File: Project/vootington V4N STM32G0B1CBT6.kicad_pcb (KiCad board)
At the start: 2 copper layers, 242.9 x 95.2 mm, 334 parts, among them J1 Conn_01x04, J2 USB_C sink board 1.3mm, J3 JST SH, J4 Pico EZmate, Q1 AP40P05, SW1 Alps SKRK, SW2 Alps SKRK, U1 SLSS49E-3, U10 SLSS49E-3, U11 SLSS49E-3, U12 SLSS49E-3, U13 SLSS49E-3, U14 SLSS49E-3, U15 SLSS49E-3, U16 SLSS49E-3, U17 SLSS49E-3, U18 SLSS49E-3, U19 SLSS49E-3, U2 SLSS49E-3, U20 SLSS49E-3, U21 SLSS49E-3, U22 SLSS49E-3, U23 SLSS49E-3, U24 SLSS49E-3, U25 SLSS49E-3, U26 SLSS49E-3, U27 SLSS49E-3, U28 SLSS49E-3, U29 SLSS49E-3, U3 SLSS49E-3, U30 SLSS49E-3, U31 SLSS49E-3, U32 SLSS49E-3, U33 SLSS49E-3, U34 SLSS49E-3, U35 SLSS49E-3, U36 SLSS49E-3, U37 SLSS49E-3, U38 SLSS49E-3, U39 SLSS49E-3, U4 SLSS49E-3, U40 SLSS49E-3, U41 SLSS49E-3, U42 SLSS49E-3, U43 SLSS49E-3, U44 SLSS49E-3, U45 SLSS49E-3, U46 SLSS49E-3, U47 SLSS49E-3, U48 SLSS49E-3, U49 SLSS49E-3, U5 SLSS49E-3, U50 SLSS49E-3, U51 SLSS49E-3, U52 SLSS49E-3, U53 STM32G0B1CBTx, U54 AP2112K-3.3, U55 PRTR5V0U2X, U56 74AHCT1G125, U57 74HC4051, U58 74HC4051, U59 74HC4051, U6 SLSS49E-3, U60 74HC4051, U61 74HC4051, U62 74HC4051, U63 74HC4051, U7 SLSS49E-3, U8 SLSS49E-3, U9 SLSS49E-3

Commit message: revision proto ready
folder clean up
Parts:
- moved G*** 82.7 mm to (132.3, 58.6)
- moved G*** 32.5 mm to (265.1, 46.8), turned to -90 degrees
- moved H9 10.3 mm to (184.2, 60.3)
- moved H16 4.83 mm to (266.7, 69.8)
- moved H14 3.59 mm to (223.8, 69.8)
- moved H13 0.79 mm to (240.5, 41.3)
- moved H1 0.79 mm to (36.5, 22.2)
- moved H6 0.38 mm to (106.7, 69.8)
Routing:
- net GND: track 318.6 -> 333.2 mm, vias 189 -> 195
- net K_36: track 30.3 -> 24.1 mm
- net K_12: track 52.9 -> 49.0 mm
- net ADC0: track 213.2 -> 216.7 mm
- net K_24: track 27.8 -> 25.0 mm
- net K_46: track 42.4 -> 39.9 mm
- net RGB MCU: track 34.8 -> 33.6 mm
- net Net-(D32-DIN): track 18.0 -> 16.8 mm
- net K_26: track 23.9 -> 22.9 mm
- net +5V: track 1292.0 -> 1291.1 mm
- net +3V3: track 259.3 -> 258.4 mm
- net K_31: track 17.9 -> 17.1 mm
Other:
- board text added: "JLCJLCJLCJLC"
- board text removed: "K47!???!!!"
- board text removed: "rearrange layout. add caps reroute and make sure multiplexers have right amount are correct rearrange mounting holes, traymount?? POWER SHIFTER, PINOUT"

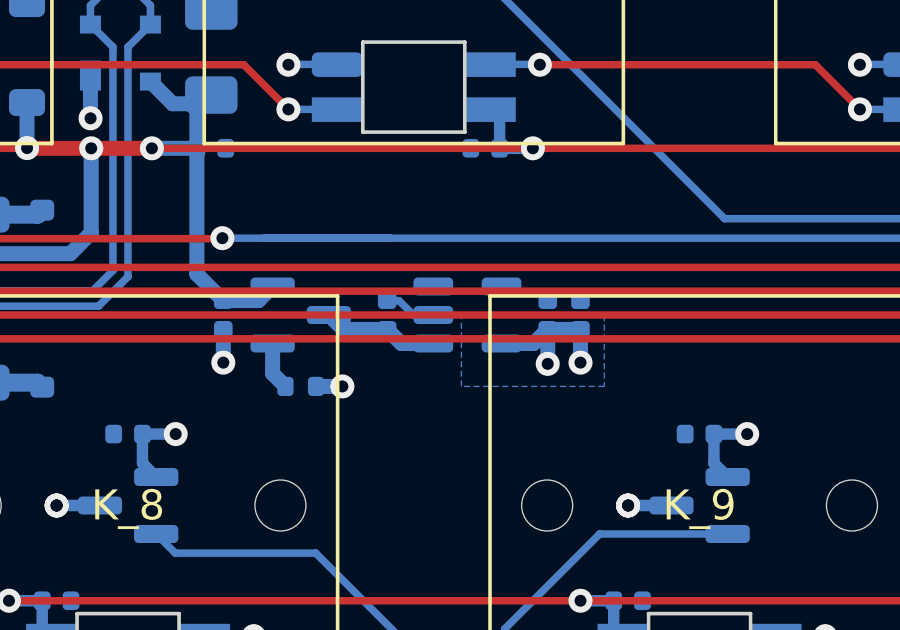
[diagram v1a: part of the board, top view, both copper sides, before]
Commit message: power error fix
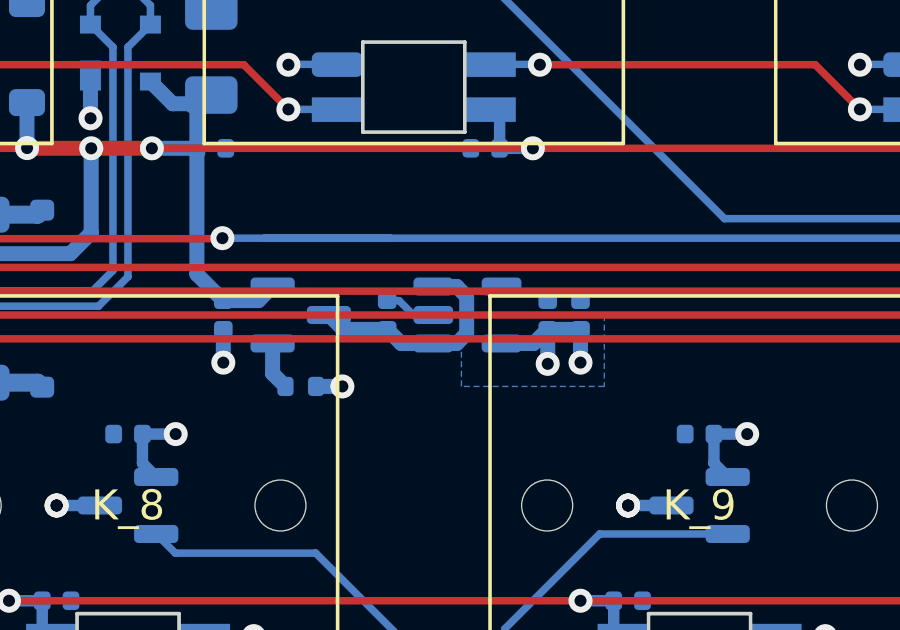
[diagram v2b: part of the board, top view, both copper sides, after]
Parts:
- moved G*** 14.1 mm to (256.4, 35.7), turned to 180 degrees
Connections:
- U54 pad 3: unconnected-(U54-EN-Pad3) -> Net-(Q1-D)
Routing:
- net Net-(Q1-D): track 3.87 -> 7.61 mm
